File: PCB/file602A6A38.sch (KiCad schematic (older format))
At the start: 27 parts, among them IC4 74LV1T125GVH, IC5 74LV1T125GVH

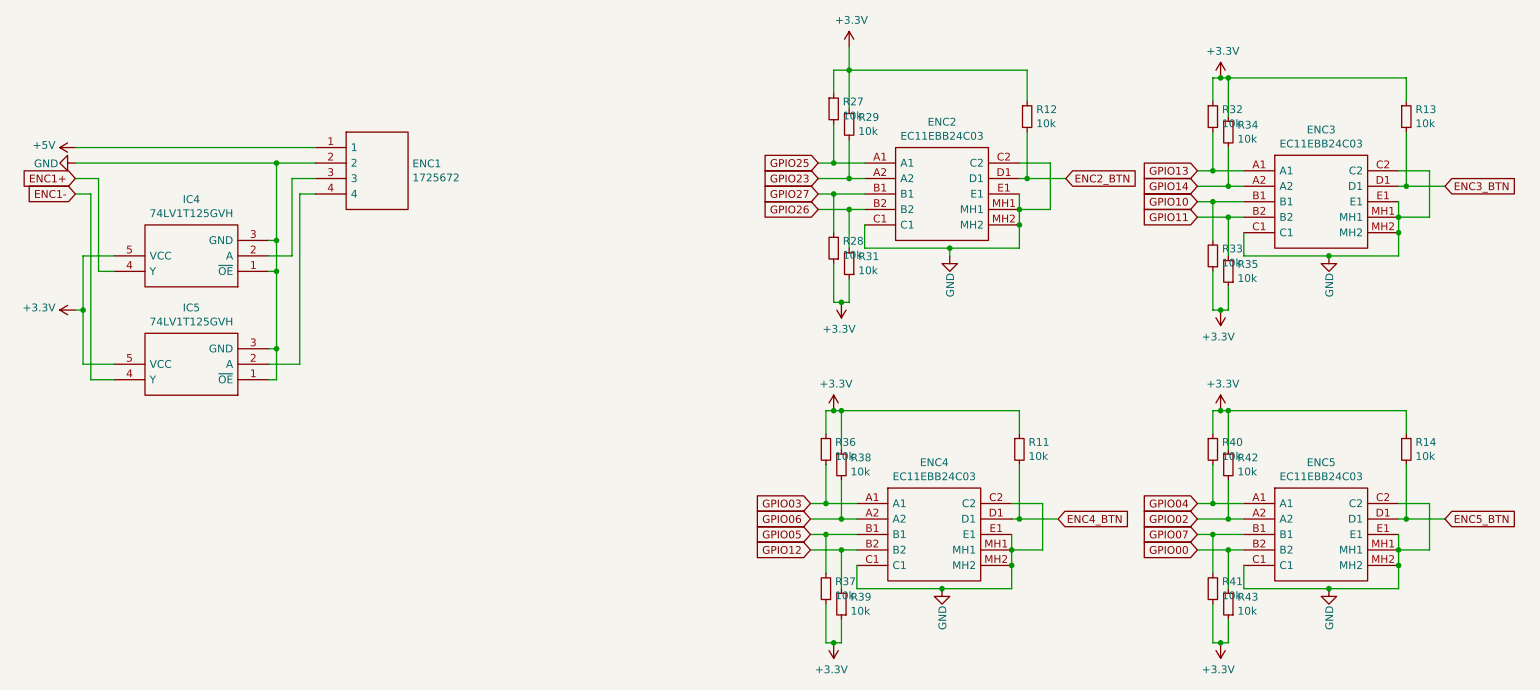
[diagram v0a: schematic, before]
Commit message: Cleaned up repository. Created a BOM in iBOM Format.
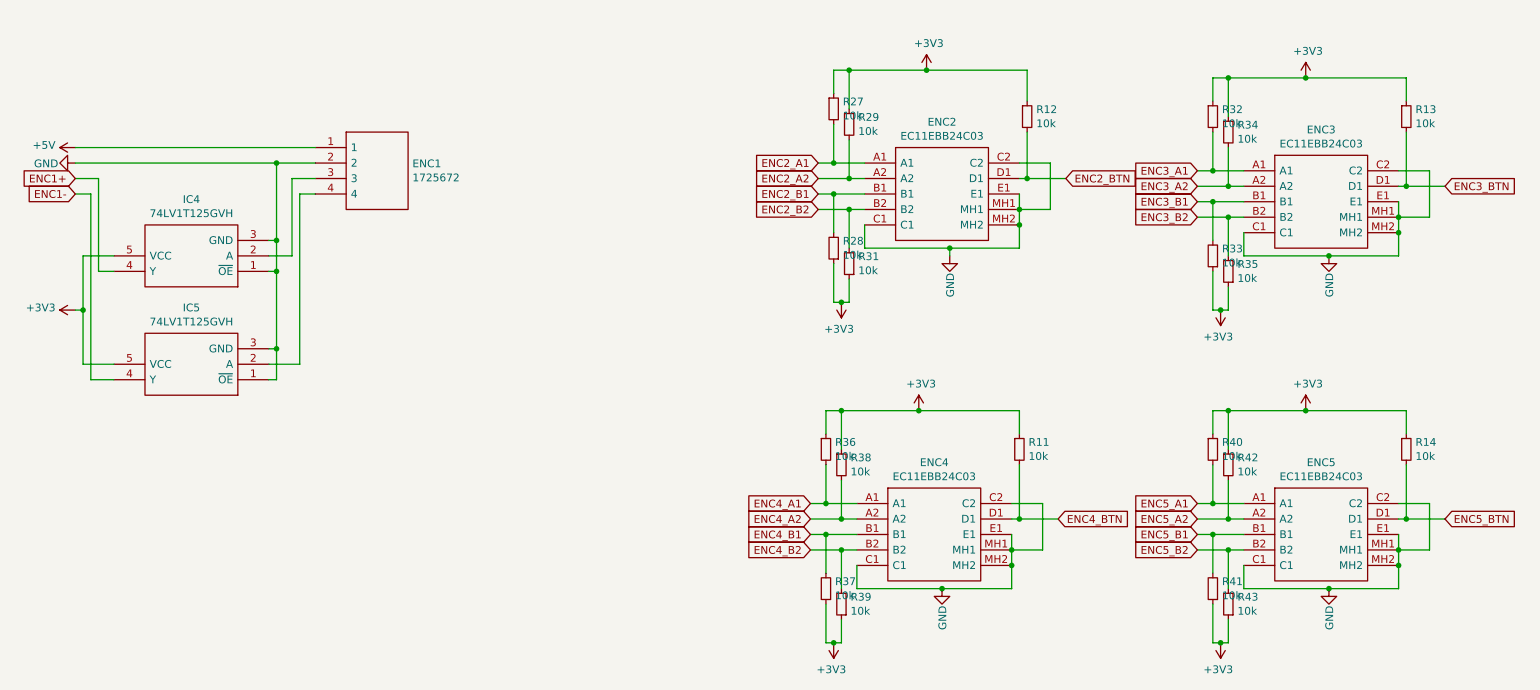
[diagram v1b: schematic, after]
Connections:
- net GPIO00 renamed ENC5_B2
- net GPIO02 renamed ENC5_A2
- net GPIO03 renamed ENC4_A1
- net GPIO04 renamed ENC5_A1
- net GPIO05 renamed ENC4_B1
- net GPIO06 renamed ENC4_A2
- net GPIO07 renamed ENC5_B1
- net GPIO10 renamed ENC3_B1
- net GPIO11 renamed ENC3_B2
- net GPIO12 renamed ENC4_B2
- net GPIO13 renamed ENC3_A1
- net GPIO14 renamed ENC3_A2
- net GPIO23 renamed ENC2_A2
- net GPIO25 renamed ENC2_A1
- net GPIO26 renamed ENC2_B2
- net GPIO27 renamed ENC2_B1
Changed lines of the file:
@@
 Wire Wire Line
 	1700 1700 1600 1700
-$Comp
-L power:+3.3V #PWR0146
-U 1 1 602CF37F
-P 1600 2450
-F 0 "#PWR0146" H 1600 2300 50  0001 C CNN
-F 1 "+3.3V" V 1615 2578 50  0000 L CNN
-F 2 "" H 1600 2450 50  0001 C CNN
-F 3 "" H 1600 2450 50  0001 C CNN
-	1    1600 2450
-	0    -1   -1   0
-$EndComp
 Wire Wire Line
 	1850 2800 1650 2800
@@
 Connection ~ 1650 2450
 Text GLabel 6400 1500 0    50   Input ~ 0
-GPIO25
+ENC2_A1
 Text GLabel 6400 1700 0    50   Input ~ 0
-GPIO27
+ENC2_B1
 $Comp
 L Device:R_Small R31
@@
 	-1   0    0    1
 $EndComp
-$Comp
-L power:+3.3V #PWR0149
-U 1 1 602DB8B1
-P 6550 2400
-F 0 "#PWR0149" H 6550 2250 50  0001 C CNN
-F 1 "+3.3V" H 6565 2573 50  0000 C CNN
-F 2 "" H 6550 2400 50  0001 C CNN
-F 3 "" H 6550 2400 50  0001 C CNN
-	1    6550 2400
-	-1   0    0    1
-$EndComp
 Wire Wire Line
 	6600 2250 6600 2400
 Wire Wire Line
-	6600 2400 6550 2400
-Wire Wire Line
 	6500 2150 6500 2400
-Wire Wire Line
-	6500 2400 6550 2400
-Connection ~ 6550 2400
 Wire Wire Line
 	6600 2050 6600 1800
@@
 	6500 1950 6500 1700
 Text GLabel 6400 1600 0    50   Input ~ 0
-GPIO23
+ENC2_A2
 Text GLabel 6400 1800 0    50   Input ~ 0
-GPIO26
+ENC2_B2
 Wire Wire Line
 	6400 1700 6500 1700
@@
 $EndComp
 Text GLabel 8850 1550 0    50   Input ~ 0
-GPIO13
+ENC3_A1
 Text GLabel 8850 1750 0    50   Input ~ 0
-GPIO10
+ENC3_B1
 $Comp
 L Device:R_Small R35
@@
 	-1   0    0    1
 $EndComp
-$Comp
-L power:+3.3V #PWR0155
-U 1 1 60302773
-P 9000 2450
-F 0 "#PWR0155" H 9000 2300 50  0001 C CNN
-F 1 "+3.3V" H 9015 2623 50  0000 C CNN
-F 2 "" H 9000 2450 50  0001 C CNN
-F 3 "" H 9000 2450 50  0001 C CNN
-	1    9000 2450
-	-1   0    0    1
-$EndComp
 Wire Wire Line
 	9050 2300 9050 2450
 Wire Wire Line
-	9050 2450 9000 2450
-Wire Wire Line
 	8950 2200 8950 2450
-Wire Wire Line
-	8950 2450 9000 2450
-Connection ~ 9000 2450
 Wire Wire Line
 	9050 2100 9050 1850
@@
 	8950 2000 8950 1750
 Text GLabel 8850 1650 0    50   Input ~ 0
-GPIO14
+ENC3_A2
 Text GLabel 8850 1850 0    50   Input ~ 0
-GPIO11
+ENC3_B2
 Wire Wire Line
 	8850 1750 8950 1750
@@
 	1    0    0    -1
 $EndComp
-$Comp
-L power:+3.3V #PWR0156
-U 1 1 60302796
-P 9000 950
-F 0 "#PWR0156" H 9000 800 50  0001 C CNN
-F 1 "+3.3V" H 9015 1123 50  0000 C CNN
-F 2 "" H 9000 950 50  0001 C CNN
-F 3 "" H 9000 950 50  0001 C CNN
-	1    9000 950
-	1    0    0    -1
-$EndComp
 Wire Wire Line
 	8950 1100 8950 950
 Wire Wire Line
-	8950 950  9000 950
-Wire Wire Line
 	9050 1200 9050 950
-Wire Wire Line
-	9050 950  9000 950
-Connection ~ 9000 950
 Wire Wire Line
 	8950 1300 8950 1550
@@
 $EndComp
 Text GLabel 6350 3900 0    50   Input ~ 0
-GPIO05
+ENC4_B1
 Text GLabel 6350 3700 0    50   Input ~ 0
-GPIO03
+ENC4_A1
 $Comp
 L Device:R_Small R39
@@
 	-1   0    0    1
 $EndComp
-$Comp
-L power:+3.3V #PWR0158
-U 1 1 6031EDC1
-P 6500 4600
-F 0 "#PWR0158" H 6500 4450 50  0001 C CNN
-F 1 "+3.3V" H 6515 4773 50  0000 C CNN
-F 2 "" H 6500 4600 50  0001 C CNN
-F 3 "" H 6500 4600 50  0001 C CNN
-	1    6500 4600
-	-1   0    0    1
-$EndComp
 Wire Wire Line
 	6550 4450 6550 4600
 Wire Wire Line
-	6550 4600 6500 4600
-Wire Wire Line
 	6450 4350 6450 4600
-Wire Wire Line
-	6450 4600 6500 4600
-Connection ~ 6500 4600
 Wire Wire Line
 	6550 4250 6550 4000
@@
 	6450 4150 6450 3900
 Text GLabel 6350 4000 0    50   Input ~ 0
-GPIO12
+ENC4_B2
 Wire Wire Line
 	6350 3900 6450 3900
@@
 	1    0    0    -1
 $EndComp
-$Comp
-L power:+3.3V #PWR0159
-U 1 1 6031EDE4
-P 6500 3100
-F 0 "#PWR0159" H 6500 2950 50  0001 C CNN
-F 1 "+3.3V" H 6515 3273 50  0000 C CNN
-F 2 "" H 6500 3100 50  0001 C CNN
-F 3 "" H 6500 3100 50  0001 C CNN
-	1    6500 3100
-	1    0    0    -1
-$EndComp
 Wire Wire Line
 	6450 3250 6450 3100
 Wire Wire Line
-	6450 3100 6500 3100
-Wire Wire Line
 	6550 3350 6550 3100
-Wire Wire Line
-	6550 3100 6500 3100
-Connection ~ 6500 3100
 Wire Wire Line
 	6450 3450 6450 3700
@@
 $EndComp
 Text GLabel 8850 3700 0    50   Input ~ 0
-GPIO04
+ENC5_A1
 Text GLabel 8850 3900 0    50   Input ~ 0
-GPIO07
+ENC5_B1
 $Comp
 L Device:R_Small R43
@@
 	-1   0    0    1
 $EndComp
-$Comp
-L power:+3.3V #PWR0160
-U 1 1 60326DE4
-P 9000 4600
-F 0 "#PWR0160" H 9000 4450 50  0001 C CNN
-F 1 "+3.3V" H 9015 4773 50  0000 C CNN
-F 2 "" H 9000 4600 50  0001 C CNN
-F 3 "" H 9000 4600 50  0001 C CNN
-	1    9000 4600
-	-1   0    0    1
-$EndComp
 Wire Wire Line
 	9050 4450 9050 4600
 Wire Wire Line
-	9050 4600 9000 4600
-Wire Wire Line
 	8950 4350 8950 4600
-Wire Wire Line
-	8950 4600 9000 4600
-Connection ~ 9000 4600
 Wire Wire Line
 	9050 4250 9050 4000
@@
 	8950 4150 8950 3900
 Text GLabel 8850 3800 0    50   Input ~ 0
-GPIO02
+ENC5_A2
 Text GLabel 8850 4000 0    50   Input ~ 0
-GPIO00
+ENC5_B2
 Wire Wire Line
 	8850 3900 8950 3900
@@
 	1    0    0    -1
 $EndComp
-$Comp
-L power:+3.3V #PWR0161
-U 1 1 60326E07
-P 9000 3100
-F 0 "#PWR0161" H 9000 2950 50  0001 C CNN
-F 1 "+3.3V" H 9015 3273 50  0000 C CNN
-F 2 "" H 9000 3100 50  0001 C CNN
-F 3 "" H 9000 3100 50  0001 C CNN
-	1    9000 3100
-	1    0    0    -1
-$EndComp
 Wire Wire Line
 	8950 3250 8950 3100
 Wire Wire Line
-	8950 3100 9000 3100
-Wire Wire Line
 	9050 3350 9050 3100
-Wire Wire Line
-	9050 3100 9000 3100
-Connection ~ 9000 3100
 Wire Wire Line
 	8950 3450 8950 3700
@@
 $EndComp
 Text GLabel 6350 3800 0    50   Input ~ 0
-GPIO06
+ENC4_A2
 Connection ~ 6600 900
 Wire Wire Line
 	6500 900  6600 900
-Wire Wire Line
-	6600 750  6600 900
-$Comp
-L power:+3.3V #PWR0151
-U 1 1 60522FD2
-P 6600 750
-F 0 "#PWR0151" H 6600 600 50  0001 C CNN
-F 1 "+3.3V" H 6615 923 50  0000 C CNN
-F 2 "" H 6600 750 50  0001 C CNN
-F 3 "" H 6600 750 50  0001 C CNN
-	1    6600 750
-	1    0    0    -1
-$EndComp
 Wire Wire Line
 	7250 2100 7250 2050
@@
 $EndComp
 Wire Wire Line
-	6600 900  7750 900
+	6600 900  7100 900
 Wire Wire Line
 	7750 900  7750 1100
@@
 Connection ~ 6550 3100
 Wire Wire Line
-	6550 3100 7700 3100
+	6550 3100 7050 3100
 Wire Wire Line
 	7700 3450 7700 3800
@@
 Connection ~ 9050 3100
 Wire Wire Line
-	9050 3100 10200 3100
+	9050 3100 9550 3100
 Wire Wire Line
 	10200 3450 10200 3800
@@
 Connection ~ 9050 950
 Wire Wire Line
-	9050 950  10200 950
+	9050 950  9550 950
 Wire Wire Line
 	10200 1300 10200 1650
@@
 	10450 3800 10200 3800
 Connection ~ 10200 3800
+$Comp
+L power:+3V3 #PWR0156
+U 1 1 603A7D0F
+P 1600 2450
+F 0 "#PWR0156" H 1600 2300 50  0001 C CNN
+F 1 "+3V3" V 1615 2578 50  0000 L CNN
+F 2 "" H 1600 2450 50  0001 C CNN
+F 3 "" H 1600 2450 50  0001 C CNN
+	1    1600 2450
+	0    -1   -1   0
+$EndComp
+Wire Wire Line
+	8950 950  9050 950
+Wire Wire Line
+	8950 2450 9000 2450
+Wire Wire Line
+	8950 3100 9050 3100
+Wire Wire Line
+	6450 3100 6550 3100
+Wire Wire Line
+	6500 2400 6550 2400
+Wire Wire Line
+	6450 4600 6500 4600
+Wire Wire Line
+	8950 4600 9000 4600
+$Comp
+L power:+3V3 #PWR0158
+U 1 1 603A8731
+P 6500 4600
+F 0 "#PWR0158" H 6500 4450 50  0001 C CNN
+F 1 "+3V3" H 6515 4773 50  0000 C CNN
+F 2 "" H 6500 4600 50  0001 C CNN
+F 3 "" H 6500 4600 50  0001 C CNN
+	1    6500 4600
+	-1   0    0    1
+$EndComp
+Connection ~ 6500 4600
+Wire Wire Line
+	6500 4600 6550 4600
+$Comp
+L power:+3V3 #PWR0159
+U 1 1 603A8F10
+P 9000 4600
+F 0 "#PWR0159" H 9000 4450 50  0001 C CNN
+F 1 "+3V3" H 9015 4773 50  0000 C CNN
+F 2 "" H 9000 4600 50  0001 C CNN
+F 3 "" H 9000 4600 50  0001 C CNN
+	1    9000 4600
+	-1   0    0    1
+$EndComp
+Connection ~ 9000 4600
+Wire Wire Line
+	9000 4600 9050 4600
+$Comp
+L power:+3V3 #PWR0160
+U 1 1 603A9385
+P 9000 2450
+F 0 "#PWR0160" H 9000 2300 50  0001 C CNN
+F 1 "+3V3" H 9015 2623 50  0000 C CNN
+F 2 "" H 9000 2450 50  0001 C CNN
+F 3 "" H 9000 2450 50  0001 C CNN
+	1    9000 2450
+	-1   0    0    1
+$EndComp
+Connection ~ 9000 2450
+Wire Wire Line
+	9000 2450 9050 2450
+$Comp
+L power:+3V3 #PWR0161
+U 1 1 603A9A9D
+P 6550 2400
+F 0 "#PWR0161" H 6550 2250 50  0001 C CNN
+F 1 "+3V3" H 6565 2573 50  0000 C CNN
+F 2 "" H 6550 2400 50  0001 C CNN
+F 3 "" H 6550 2400 50  0001 C CNN
+	1    6550 2400
+	-1   0    0    1
+$EndComp
+Connection ~ 6550 2400
+Wire Wire Line
+	6550 2400 6600 2400
+$Comp
+L power:+3V3 #PWR0163
+U 1 1 603AA07F
+P 7100 900
+F 0 "#PWR0163" H 7100 750 50  0001 C CNN
+F 1 "+3V3" H 7115 1073 50  0000 C CNN
+F 2 "" H 7100 900 50  0001 C CNN
+F 3 "" H 7100 900 50  0001 C CNN
+	1    7100 900
+	1    0    0    -1
+$EndComp
+$Comp
+L power:+3V3 #PWR0165
+U 1 1 603AA7DE
+P 9550 950
+F 0 "#PWR0165" H 9550 800 50  0001 C CNN
+F 1 "+3V3" H 9565 1123 50  0000 C CNN
+F 2 "" H 9550 950 50  0001 C CNN
+F 3 "" H 9550 950 50  0001 C CNN
+	1    9550 950
+	1    0    0    -1
+$EndComp
+$Comp
+L power:+3V3 #PWR0166
+U 1 1 603AAF03
+P 9550 3100
+F 0 "#PWR0166" H 9550 2950 50  0001 C CNN
+F 1 "+3V3" H 9565 3273 50  0000 C CNN
+F 2 "" H 9550 3100 50  0001 C CNN
+F 3 "" H 9550 3100 50  0001 C CNN
+	1    9550 3100
+	1    0    0    -1
+$EndComp
+Connection ~ 9550 3100
+Wire Wire Line
+	9550 3100 10200 3100
+$Comp
+L power:+3V3 #PWR0167
+U 1 1 603ABE8E
+P 7050 3100
+F 0 "#PWR0167" H 7050 2950 50  0001 C CNN
+F 1 "+3V3" H 7065 3273 50  0000 C CNN
+F 2 "" H 7050 3100 50  0001 C CNN
+F 3 "" H 7050 3100 50  0001 C CNN
+	1    7050 3100
+	1    0    0    -1
+$EndComp
+Connection ~ 7050 3100
+Wire Wire Line
+	7050 3100 7700 3100
+Connection ~ 9550 950
+Wire Wire Line
+	9550 950  10200 950
+Connection ~ 7100 900
+Wire Wire Line
+	7100 900  7750 900
 $EndSCHEMATC
